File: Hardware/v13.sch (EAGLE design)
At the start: 90 parts, among them J1 22-27-2081-08, J2 22-27-2031-03

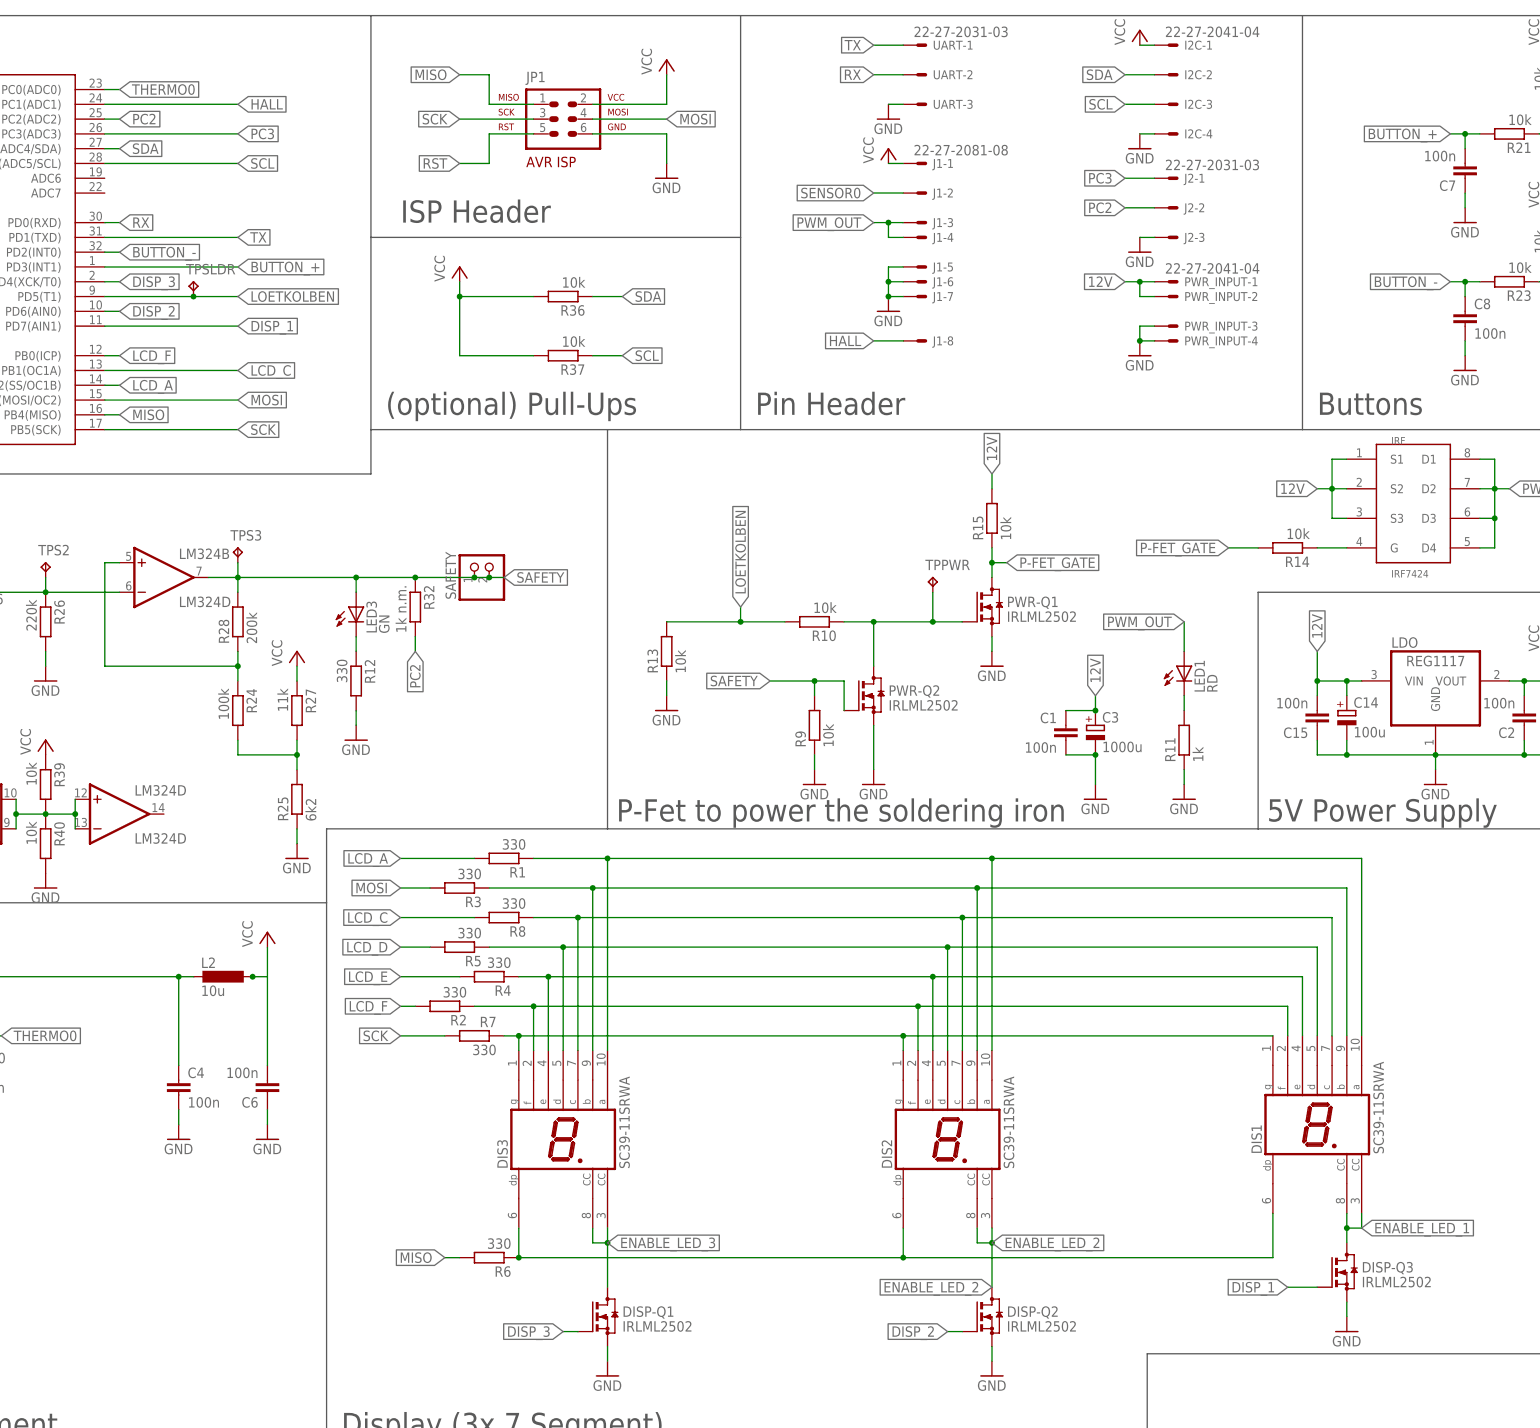
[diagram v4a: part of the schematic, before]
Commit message: added unmounted resistors around hall sensor wire added more labels changed some wires to comply with elecrow drc added heat sink for low drop, which is not connected to anything else
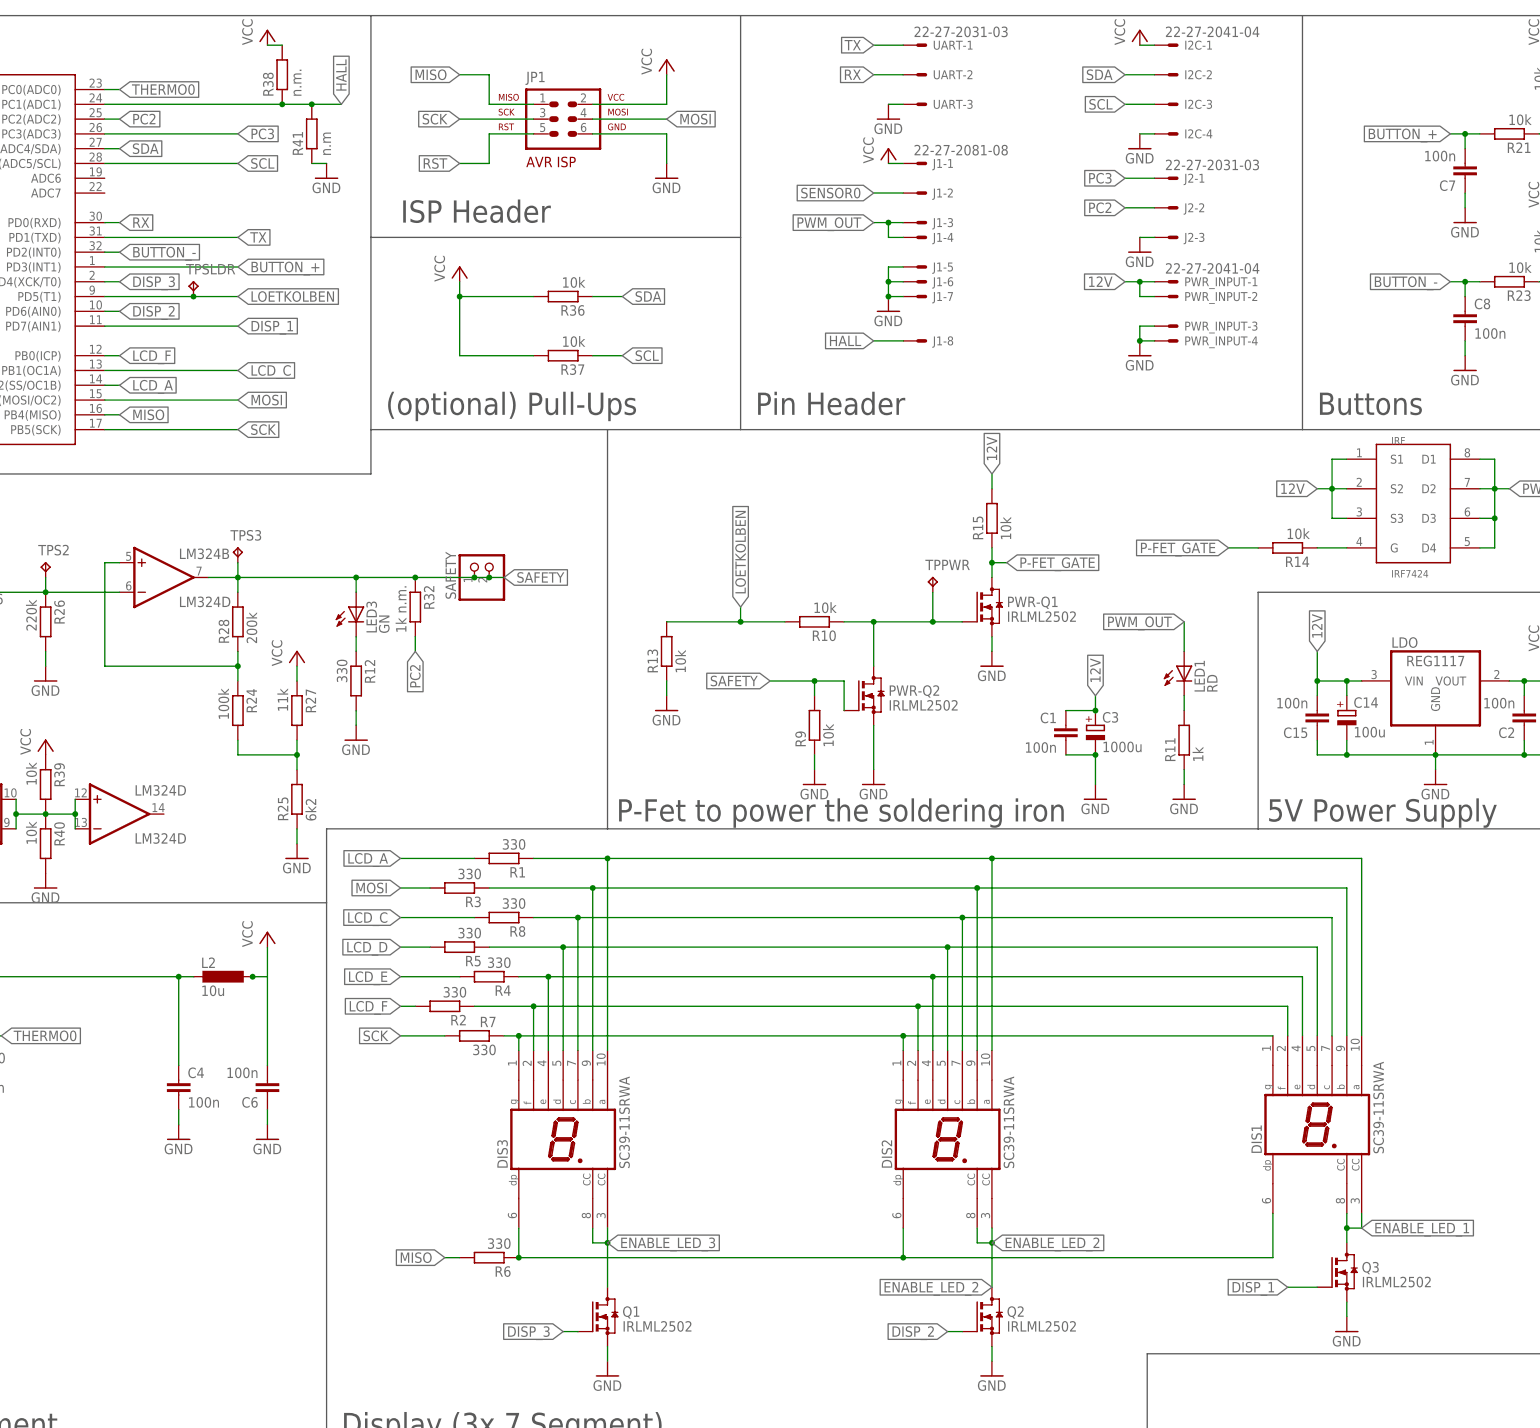
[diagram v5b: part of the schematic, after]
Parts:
- added R38: n.m., rcl:R-EU_R0603
- added R41: n.m, rcl:R-EU_R0603
- renumbered DISP-Q1 to Q1, DISP-Q2 to Q2, DISP-Q3 to Q3
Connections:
- net GND: now also R41.1
- net HALL: now also R38.1, R41.2
- net VCC: now also R38.2
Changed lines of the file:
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@@
 <part name="IRF" library="MyLib" deviceset="IRF7424" device=""/>
 <part name="GND5" library="supply1" deviceset="GND" device=""/>
-<part name="DISP-Q1" library="transistor-small-signal" deviceset="BSS123" device="" value="IRLML2502"/>
-<part name="DISP-Q2" library="transistor-small-signal" deviceset="BSS123" device="" value="IRLML2502"/>
-<part name="DISP-Q3" library="transistor-small-signal" deviceset="BSS123" device="" value="IRLML2502"/>
+<part name="Q1" library="transistor-small-signal" deviceset="BSS123" device="" value="IRLML2502"/>
+<part name="Q2" library="transistor-small-signal" deviceset="BSS123" device="" value="IRLML2502"/>
+<part name="Q3" library="transistor-small-signal" deviceset="BSS123" device="" value="IRLML2502"/>
 <part name="GND10" library="supply1" deviceset="GND" device=""/>
 <part name="C13" library="rcl" deviceset="CPOL-EU" device="E2-5" value="100u"/>
@@
 <part name="P+14" library="supply1" deviceset="VCC" device=""/>
 <part name="GND35" library="supply1" deviceset="GND" device=""/>
+<part name="R38" library="rcl" deviceset="R-EU_" device="R0603" value="n.m."/>
+<part name="R41" library="rcl" deviceset="R-EU_" device="R0603" value="n.m"/>
+<part name="P+15" library="supply1" deviceset="VCC" device=""/>
+<part name="GND36" library="supply1" deviceset="GND" device=""/>
 </parts>
 <sheets>
@@
 <instance part="IRF" gate="G$1" x="312.42" y="154.94"/>
 <instance part="GND5" gate="1" x="287.02" y="195.58"/>
-<instance part="DISP-Q1" gate="G$1" x="195.58" y="30.48"/>
-<instance part="DISP-Q2" gate="G$1" x="261.62" y="30.48"/>
-<instance part="DISP-Q3" gate="G$1" x="322.58" y="38.1"/>
+<instance part="Q1" gate="G$1" x="195.58" y="30.48"/>
+<instance part="Q2" gate="G$1" x="261.62" y="30.48"/>
+<instance part="Q3" gate="G$1" x="322.58" y="38.1"/>
 <instance part="GND10" gate="1" x="322.58" y="27.94"/>
 <instance part="C13" gate="G$1" x="358.14" y="134.62"/>
@@
 <instance part="P+14" gate="VCC" x="99.06" y="129.54"/>
 <instance part="GND35" gate="1" x="99.06" y="104.14"/>
+<instance part="R38" gate="G$1" x="139.7" y="243.84" rot="R90"/>
+<instance part="R41" gate="G$1" x="144.78" y="233.68" rot="R90"/>
+<instance part="P+15" gate="VCC" x="137.16" y="251.46"/>
+<instance part="GND36" gate="1" x="147.32" y="226.06"/>
 </instances>
 <busses>
@@
 <pinref part="R39" gate="G$1" pin="1"/>
 <pinref part="P+14" gate="VCC" pin="VCC"/>
+</segment>
+<segment>
+<pinref part="R38" gate="G$1" pin="2"/>
+<pinref part="P+15" gate="VCC" pin="VCC"/>
+<wire x1="139.7" y1="248.92" x2="137.16" y2="248.92" width="0.1524" layer="91"/>
 </segment>
 </net>
@@
 </segment>
 <segment>
-<pinref part="DISP-Q3" gate="G$1" pin="S"/>
+<pinref part="Q3" gate="G$1" pin="S"/>
 <pinref part="GND10" gate="1" pin="GND"/>
 <wire x1="322.58" y1="30.48" x2="322.58" y2="33.02" width="0.1524" layer="91"/>
@@
 </segment>
 <segment>
-<pinref part="DISP-Q2" gate="G$1" pin="S"/>
+<pinref part="Q2" gate="G$1" pin="S"/>
 <pinref part="GND24" gate="1" pin="GND"/>
 <wire x1="261.62" y1="25.4" x2="261.62" y2="22.86" width="0.1524" layer="91"/>
 </segment>
 <segment>
-<pinref part="DISP-Q1" gate="G$1" pin="S"/>
+<pinref part="Q1" gate="G$1" pin="S"/>
 <wire x1="195.58" y1="25.4" x2="195.58" y2="22.86" width="0.1524" layer="91"/>
 <pinref part="GND25" gate="1" pin="GND"/>
@@
 <pinref part="GND35" gate="1" pin="GND"/>
 </segment>
+<segment>
+<pinref part="R41" gate="G$1" pin="1"/>
+<pinref part="GND36" gate="1" pin="GND"/>
+<wire x1="147.32" y1="228.6" x2="144.78" y2="228.6" width="0.1524" layer="91"/>
+</segment>
 </net>
 <net name="N$1" class="0">
@@
 <wire x1="259.08" y1="43.18" x2="259.08" y2="45.72" width="0.1524" layer="91"/>
 <wire x1="259.08" y1="43.18" x2="261.62" y2="43.18" width="0.1524" layer="91"/>
-<pinref part="DISP-Q2" gate="G$1" pin="D"/>
+<pinref part="Q2" gate="G$1" pin="D"/>
 <label x="261.62" y="35.56" size="1.778" layer="95" rot="R180" xref="yes"/>
 <wire x1="261.62" y1="43.18" x2="261.62" y2="35.56" width="0.1524" layer="91"/>
@@
 <net name="ENABLE_LED_3" class="0">
 <segment>
-<pinref part="DISP-Q1" gate="G$1" pin="D"/>
+<pinref part="Q1" gate="G$1" pin="D"/>
 <pinref part="DIS3" gate="G$1" pin="CC"/>
 <wire x1="193.04" y1="43.18" x2="193.04" y2="45.72" width="0.1524" layer="91"/>
@@
 <pinref part="DIS1" gate="G$1" pin="CC"/>
 <wire x1="322.58" y1="48.26" x2="322.58" y2="45.72" width="0.1524" layer="91"/>
-<pinref part="DISP-Q3" gate="G$1" pin="D"/>
+<pinref part="Q3" gate="G$1" pin="D"/>
 <label x="325.12" y="45.72" size="1.778" layer="95" xref="yes"/>
 <junction x="322.58" y="45.72"/>
@@
 <net name="DISP_1" class="0">
 <segment>
-<pinref part="DISP-Q3" gate="G$1" pin="G"/>
+<pinref part="Q3" gate="G$1" pin="G"/>
 <wire x1="312.42" y1="35.56" x2="317.5" y2="35.56" width="0.1524" layer="91"/>
 <label x="312.42" y="35.56" size="1.778" layer="95" rot="R180" xref="yes"/>
@@
 <net name="DISP_3" class="0">
 <segment>
-<pinref part="DISP-Q1" gate="G$1" pin="G"/>
+<pinref part="Q1" gate="G$1" pin="G"/>
 <wire x1="187.96" y1="27.94" x2="190.5" y2="27.94" width="0.1524" layer="91"/>
 <label x="187.96" y="27.94" size="1.778" layer="95" rot="R180" xref="yes"/>
@@
 <net name="DISP_2" class="0">
 <segment>
-<pinref part="DISP-Q2" gate="G$1" pin="G"/>
+<pinref part="Q2" gate="G$1" pin="G"/>
 <wire x1="254" y1="27.94" x2="256.54" y2="27.94" width="0.1524" layer="91"/>
 <label x="254" y="27.94" size="1.778" layer="95" rot="R180" xref="yes"/>
@@
 <segment>
 <pinref part="AVR" gate="G$1" pin="PC1(ADC1)"/>
-<label x="132.08" y="238.76" size="1.778" layer="95" xref="yes"/>
-<wire x1="132.08" y1="238.76" x2="109.22" y2="238.76" width="0.1524" layer="91"/>
-</segment>
-<segment>
+<label x="149.86" y="238.76" size="1.778" layer="95" rot="R90" xref="yes"/>
+<wire x1="149.86" y1="238.76" x2="144.78" y2="238.76" width="0.1524" layer="91"/>
+<pinref part="R38" gate="G$1" pin="1"/>
+<wire x1="144.78" y1="238.76" x2="139.7" y2="238.76" width="0.1524" layer="91"/>
+<wire x1="139.7" y1="238.76" x2="109.22" y2="238.76" width="0.1524" layer="91"/>
+<junction x="139.7" y="238.76"/>
+<pinref part="R41" gate="G$1" pin="2"/>
+<junction x="144.78" y="238.76"/>
+</segment>
+<segment>
